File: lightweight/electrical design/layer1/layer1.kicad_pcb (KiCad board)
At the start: 2 copper layers, 208 x 198.4 mm, 228 parts, among them J1 XT30-F, J10 Conn_01x02_Pin, J11 Conn_01x01_Socket, J12 Conn_01x01_Socket, J13 SH1.0 5P, J14 SH1.0 3P, J15 Conn_01x01_Socket, J2 Conn_01x01_Socket, J3 Conn_01x01_Socket, J4 XT30PW-F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

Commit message: update lw pcbs
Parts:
- removed H13, H5: MountingHole, MountingHole:MountingHole_3.2mm_M3_Pad
- moved J2 45.2 mm to (113.5, 136.5), turned to 90 degrees
- moved J15 43.3 mm to (112.5, 184.7)
- moved J4 25.0 mm to (138.0, 189.1)
- moved C34 21.1 mm to (131.2, 176.8)
- moved R33 21.1 mm to (131.2, 178.6)
- moved R35 21.1 mm to (131.2, 175.1)
- moved Q2 21.0 mm to (128.4, 184.8)
- moved Q1 20.8 mm to (138.7, 181.1)
- moved R40 20.1 mm to (119.9, 183.8)
- moved D1 20.0 mm to (112.7, 175.1)
- moved D2 19.9 mm to (112.7, 180.1)
- moved R34 14.4 mm to (134.0, 172.8)
- moved J1 10.4 mm to (73.7, 194.1)
- moved J6 10.4 mm to (81.2, 192.1)
- moved TP2 10.4 mm to (69.2, 189.1)
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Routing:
- net /LED: track 475.1 -> 3.90 mm, vias 15 -> 14
- net +12V: track 119.3 -> 58.8 mm, vias 0 -> 2
- net +48V: track 89.2 -> 34.6 mm, vias 5 -> 0
- net VCCQ: track 463.9 -> 450.1 mm
- net /SOLENOIDON: track 107.6 -> 99.0 mm
- net +3V3: track 295.5 -> 302.5 mm
- net Net-(Q1-G): track 7.33 -> 11.0 mm
- net Net-(U1-I5): track 37.9 -> 35.0 mm
- net Net-(U2-I4): track 41.7 -> 39.1 mm
- net /BALL: track 109.6 -> 107.1 mm
- net GND: track 220.9 -> 223.2 mm, vias 97 -> 92
- net Net-(U1-I6): track 33.2 -> 31.0 mm
- net Net-(Q1-S): track 17.7 -> 15.5 mm
- net Net-(U1-I3): track 44.9 -> 43.1 mm
- net Net-(U2-I9): track 33.4 -> 31.9 mm
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- added copper zone on F.Cu, net +48V
- added copper zone on B.Cu, net /LED
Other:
- outline, holes or cut-outs redrawn

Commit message: update lw l3 pcb
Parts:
- moved TP3 5.08 mm to (31.0, 97.1), turned to 90 degrees
- moved TP4 5.08 mm to (31.0, 118.1), turned to 90 degrees
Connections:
- BUCK1 pad 1: VCCQ -> +12V
- BUCK1 pad 3: +12V -> +5V
- BUCK2 pad 1: +3V3 -> +12V
- BUCK2 pad 3: +12V -> +3V3
- TP3 pad 1: VCCQ -> +5V
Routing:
- net +5V: track 8.00 -> 170.4 mm, vias 0 -> 4
- net GND: track 223.2 -> 236.8 mm
- net VCCQ: track 450.1 -> 437.7 mm, vias 0 -> 1
- net +3V3: track 302.5 -> 305.3 mm
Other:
- board text removed: "+3V3"
- board text removed: "VCCQ"

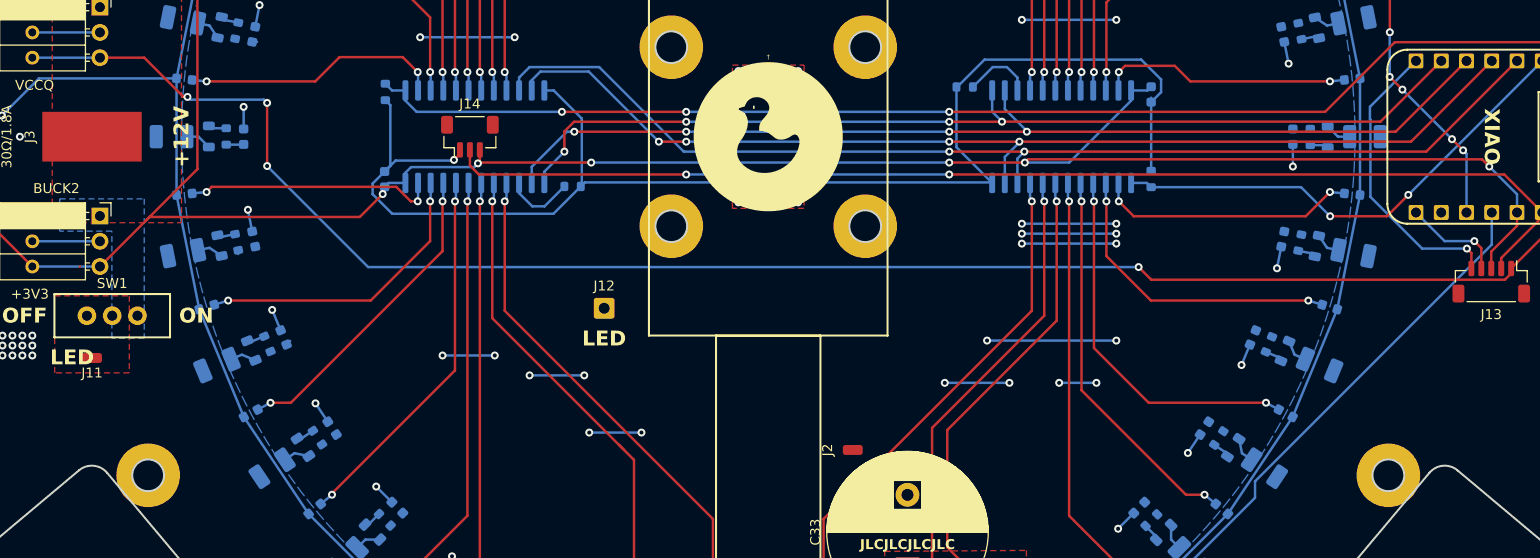
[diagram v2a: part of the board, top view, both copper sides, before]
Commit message: fix drc faults on l1, l2, and l3 pcbs
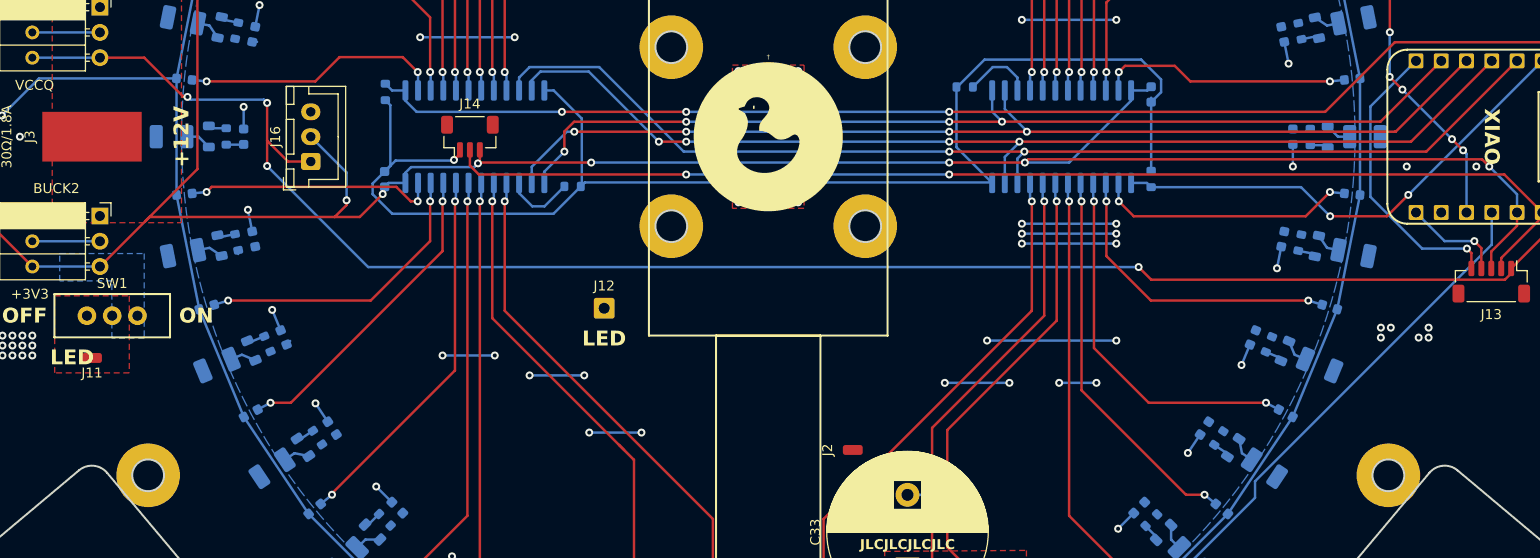
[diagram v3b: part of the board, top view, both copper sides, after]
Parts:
- added J16: Conn_01x03_Pin, Connector_JST:JST_XH_B3B-XH-A_1x03_P2.50mm_Vertical, F.Cu at (59.0, 107.5)
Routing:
- net +3V3: track 305.3 -> 315.4 mm, vias 6 -> 7
- net GND: track 236.8 -> 242.3 mm, vias 92 -> 101
- net +5V: track 170.4 -> 175.7 mm

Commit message: add lw pcb files
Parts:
- moved C11 28.3 mm to (76.3, 145.2)
- moved C19 28.3 mm to (145.2, 173.7)
- moved C23 28.3 mm to (173.7, 145.2)
- moved C31 28.3 mm to (145.2, 76.3)
- moved D1 28.3 mm to (132.7, 195.1)
- moved D2 28.3 mm to (132.7, 200.1)
- moved L11 28.3 mm to (73.0, 146.5)
- moved L12 28.3 mm to (78.2, 156.2)
- moved L3 28.3 mm to (103.5, 73.0)
- moved L4 28.3 mm to (93.8, 78.2)
- moved L8 28.3 mm to (69.8, 114.0)
- moved LDR17 28.3 mm to (130.8, 183.7)
- moved LDR8 28.3 mm to (66.3, 119.2)
- moved LDR9 28.3 mm to (66.3, 130.8)
- moved R10 28.3 mm to (71.5, 135.6)
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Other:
- outline, holes or cut-outs redrawn
- board text removed: "+48V"
